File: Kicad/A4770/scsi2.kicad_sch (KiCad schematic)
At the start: 27 parts, among them U9 LSI53C770 SCSI Host Controller

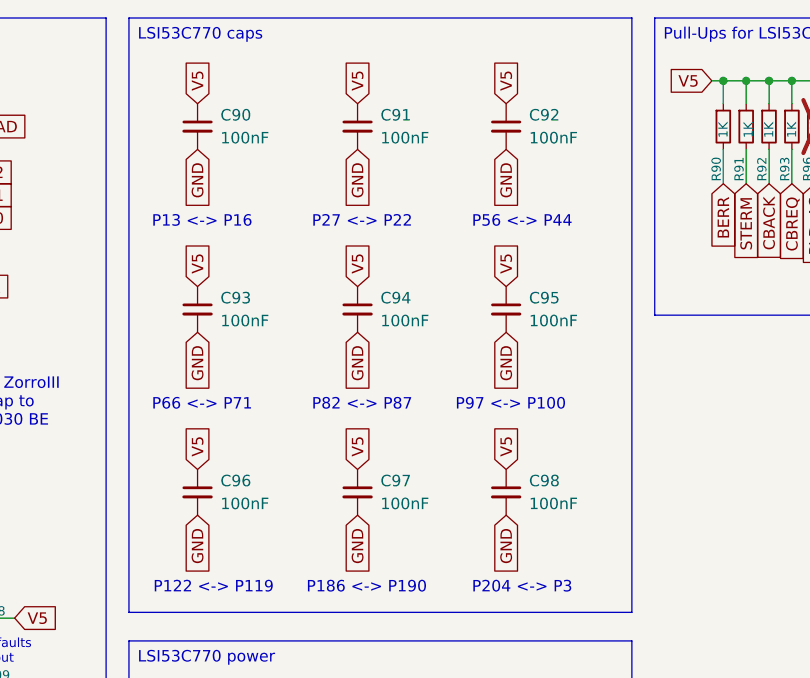
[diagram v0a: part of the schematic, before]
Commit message: Fix issues detected by JLCPCB's uploader
- Use alternating decoupling caps of 0.01uF and 0.1uF on the
  NCR53c770 as was done on the A4091 design.
- Remove DNP parts from BOM
- Remove fiducials from position files.
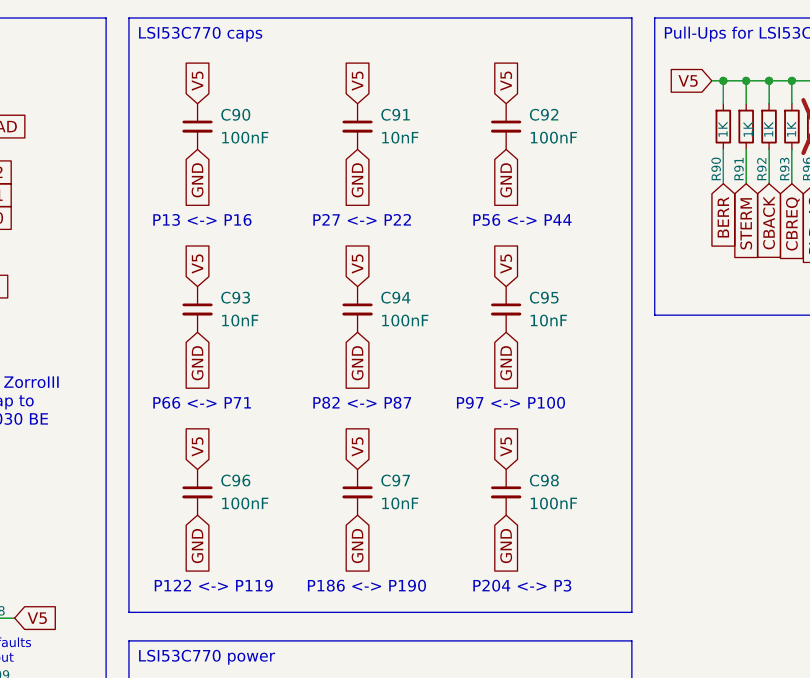
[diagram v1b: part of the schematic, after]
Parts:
- C91, C93, C95, C97: value 100nF -> 10nF
- R96, R99: now left out of the parts list
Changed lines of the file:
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@@
 			)
 		)
-		(property "Value" "100nF"
+		(property "Value" "10nF"
 			(at 196.85 48.2662 0)
 			(effects
@@
 			)
 		)
-		(property "Value" "100nF"
+		(property "Value" "10nF"
 			(at 214.63 68.5862 0)
 			(effects
@@
 		(unit 1)
 		(exclude_from_sim no)
-		(in_bom yes)
+		(in_bom no)
 		(on_board yes)
 		(dnp yes)
@@
 		(unit 1)
 		(exclude_from_sim no)
-		(in_bom yes)
+		(in_bom no)
 		(on_board yes)
 		(dnp yes)
@@
 			)
 		)
-		(property "Value" "100nF"
+		(property "Value" "10nF"
 			(at 231.14 48.2662 0)
 			(effects
@@
 			)
 		)
-		(property "Value" "100nF"
+		(property "Value" "10nF"
 			(at 214.63 27.9462 0)
 			(effects

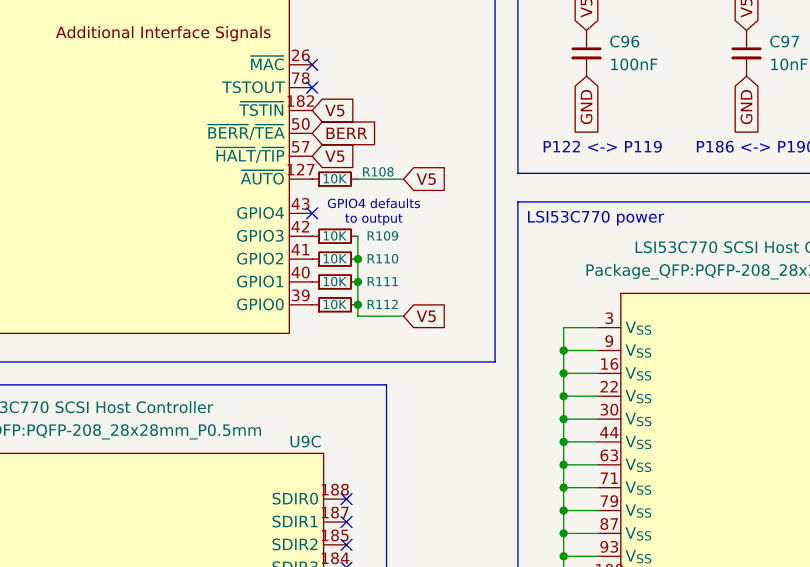
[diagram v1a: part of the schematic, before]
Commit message: Changes from schematics review 26-02-08
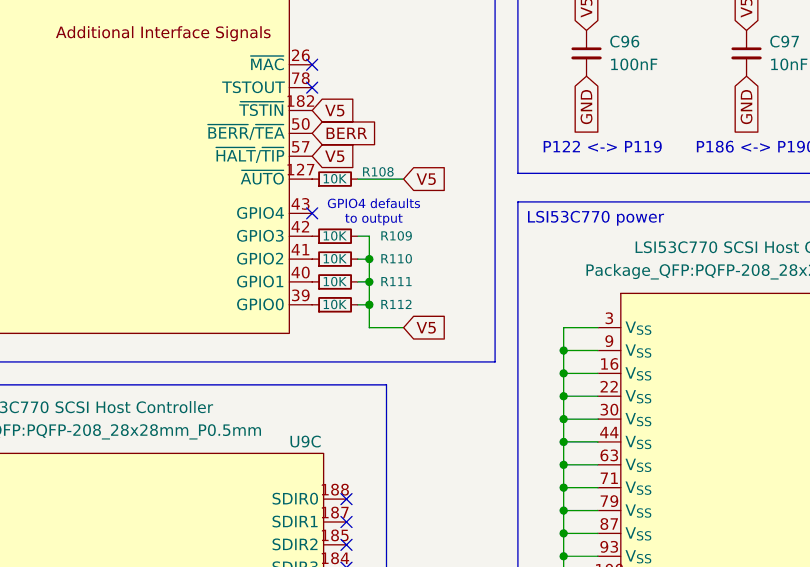
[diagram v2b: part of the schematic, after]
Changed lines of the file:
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@@
 	)
 	(junction
+		(at 170.18 92.71)
+		(diameter 0)
+		(color 0 0 0 0)
+	)
+	(junction
 		(at 233.68 115.57)
 		(diameter 0)
@@
 	)
 	(junction
+		(at 170.18 95.25)
+		(diameter 0)
+		(color 0 0 0 0)
+	)
+	(junction
 		(at 191.77 133.35)
 		(diameter 0)
@@
 	)
 	(junction
-		(at 168.91 90.17)
-		(diameter 0)
-		(color 0 0 0 0)
-	)
-	(junction
 		(at 267.97 21.59)
 		(diameter 0)
@@
 	)
 	(junction
-		(at 191.77 105.41)
+		(at 170.18 90.17)
 		(diameter 0)
 		(color 0 0 0 0)
 	)
 	(junction
-		(at 191.77 115.57)
+		(at 191.77 105.41)
 		(diameter 0)
 		(color 0 0 0 0)
 	)
 	(junction
-		(at 191.77 123.19)
+		(at 191.77 115.57)
 		(diameter 0)
 		(color 0 0 0 0)
 	)
 	(junction
-		(at 168.91 95.25)
+		(at 191.77 123.19)
 		(diameter 0)
 		(color 0 0 0 0)
@@
 	)
 	(junction
-		(at 168.91 92.71)
-		(diameter 0)
-		(color 0 0 0 0)
-	)
-	(junction
 		(at 233.68 107.95)
 		(diameter 0)
@@
 	(wire
 		(pts
-			(xy 168.91 90.17) (xy 168.91 92.71)
+			(xy 170.18 90.17) (xy 170.18 92.71)
 		)
 		(stroke
@@
 	(wire
 		(pts
-			(xy 168.91 92.71) (xy 168.91 95.25)
+			(xy 170.18 92.71) (xy 170.18 95.25)
 		)
 		(stroke
@@
 	(wire
 		(pts
-			(xy 173.99 96.52) (xy 168.91 96.52)
+			(xy 173.99 97.79) (xy 170.18 97.79)
 		)
 		(stroke
@@
 	(wire
 		(pts
+			(xy 170.18 87.63) (xy 168.91 87.63)
+		)
+		(stroke
+			(width 0)
+			(type default)
+		)
+	)
+	(wire
+		(pts
 			(xy 191.77 140.97) (xy 195.58 140.97)
 		)
@@
 	(wire
 		(pts
+			(xy 170.18 90.17) (xy 168.91 90.17)
+		)
+		(stroke
+			(width 0)
+			(type default)
+		)
+	)
+	(wire
+		(pts
 			(xy 191.77 135.89) (xy 195.58 135.89)
 		)
@@
 	(wire
 		(pts
+			(xy 170.18 95.25) (xy 168.91 95.25)
+		)
+		(stroke
+			(width 0)
+			(type default)
+		)
+	)
+	(wire
+		(pts
 			(xy 231.14 115.57) (xy 233.68 115.57)
 		)
@@
 	(wire
 		(pts
-			(xy 168.91 87.63) (xy 168.91 90.17)
+			(xy 170.18 87.63) (xy 170.18 90.17)
 		)
 		(stroke
@@
 	(wire
 		(pts
-			(xy 168.91 96.52) (xy 168.91 95.25)
+			(xy 170.18 97.79) (xy 170.18 95.25)
+		)
+		(stroke
+			(width 0)
+			(type default)
+		)
+	)
+	(wire
+		(pts
+			(xy 170.18 92.71) (xy 168.91 92.71)
 		)
 		(stroke
@@
 	(global_label "V5"
 		(shape input)
-		(at 173.99 96.52 0)
+		(at 173.99 97.79 0)
 		(fields_autoplaced yes)
 		(effects
@@
 		)
 		(property "Intersheetrefs" "${INTERSHEET_REFS}"
-			(at 179.2733 96.52 0)
+			(at 179.2733 97.79 0)
 			(effects
 				(font
@@
 		(dnp no)
 		(property "Reference" "R112"
-			(at 173.482 95.25 90)
+			(at 175.006 95.25 90)
 			(effects
 				(font
@@
 		(dnp no)
 		(property "Reference" "R111"
-			(at 173.482 92.71 90)
+			(at 175.006 92.71 90)
 			(effects
 				(font
@@
 		(dnp no)
 		(property "Reference" "R109"
-			(at 173.482 87.63 90)
+			(at 175.006 87.63 90)
 			(effects
 				(font
@@
 		(dnp no)
 		(property "Reference" "R110"
-			(at 173.482 90.17 90)
+			(at 175.006 90.17 90)
 			(effects
 				(font
